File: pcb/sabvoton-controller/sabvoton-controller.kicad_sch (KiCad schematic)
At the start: 1 part

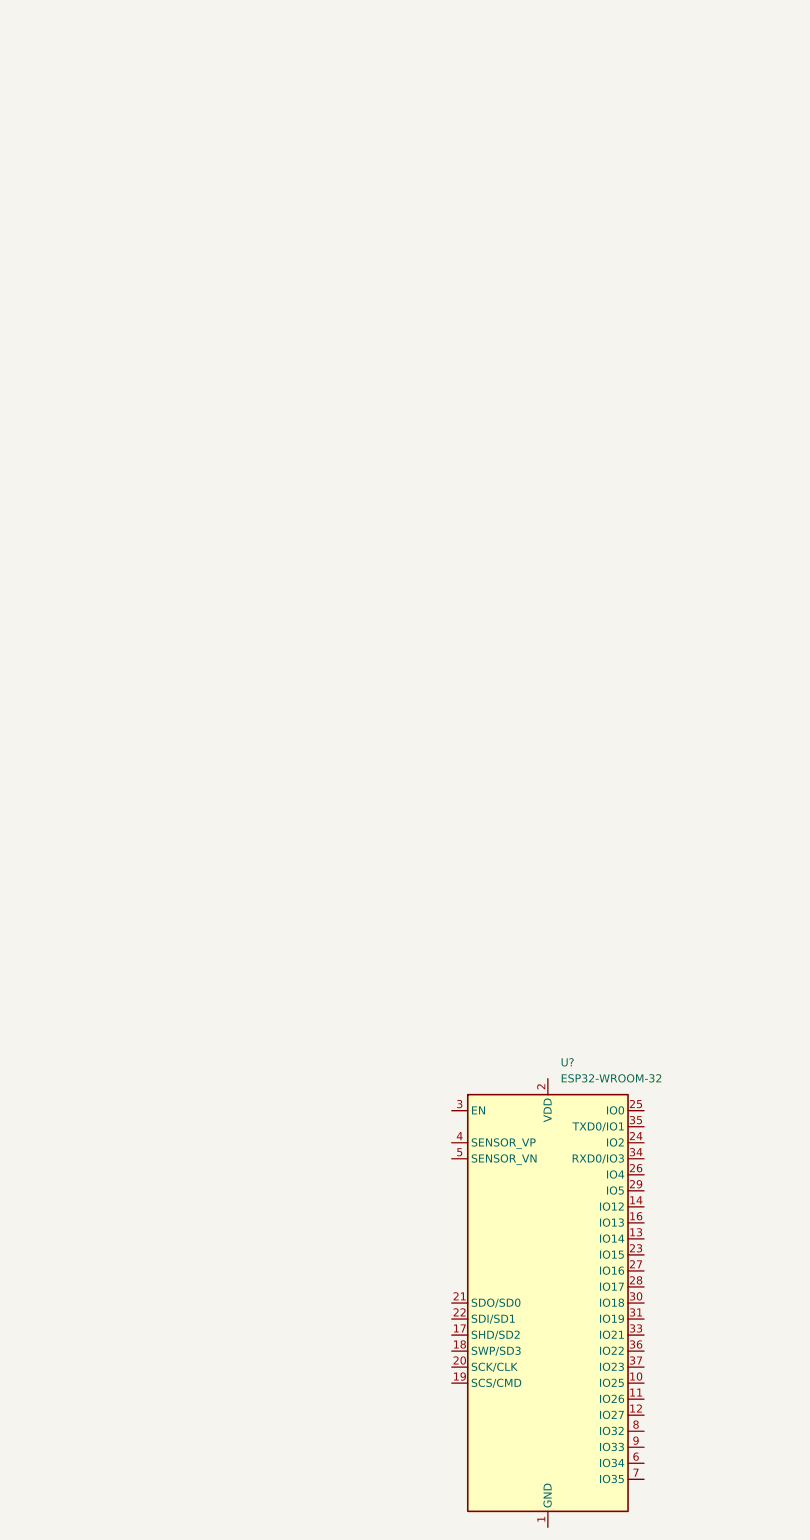
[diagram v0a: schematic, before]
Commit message: Added controller connectors && microcontroller
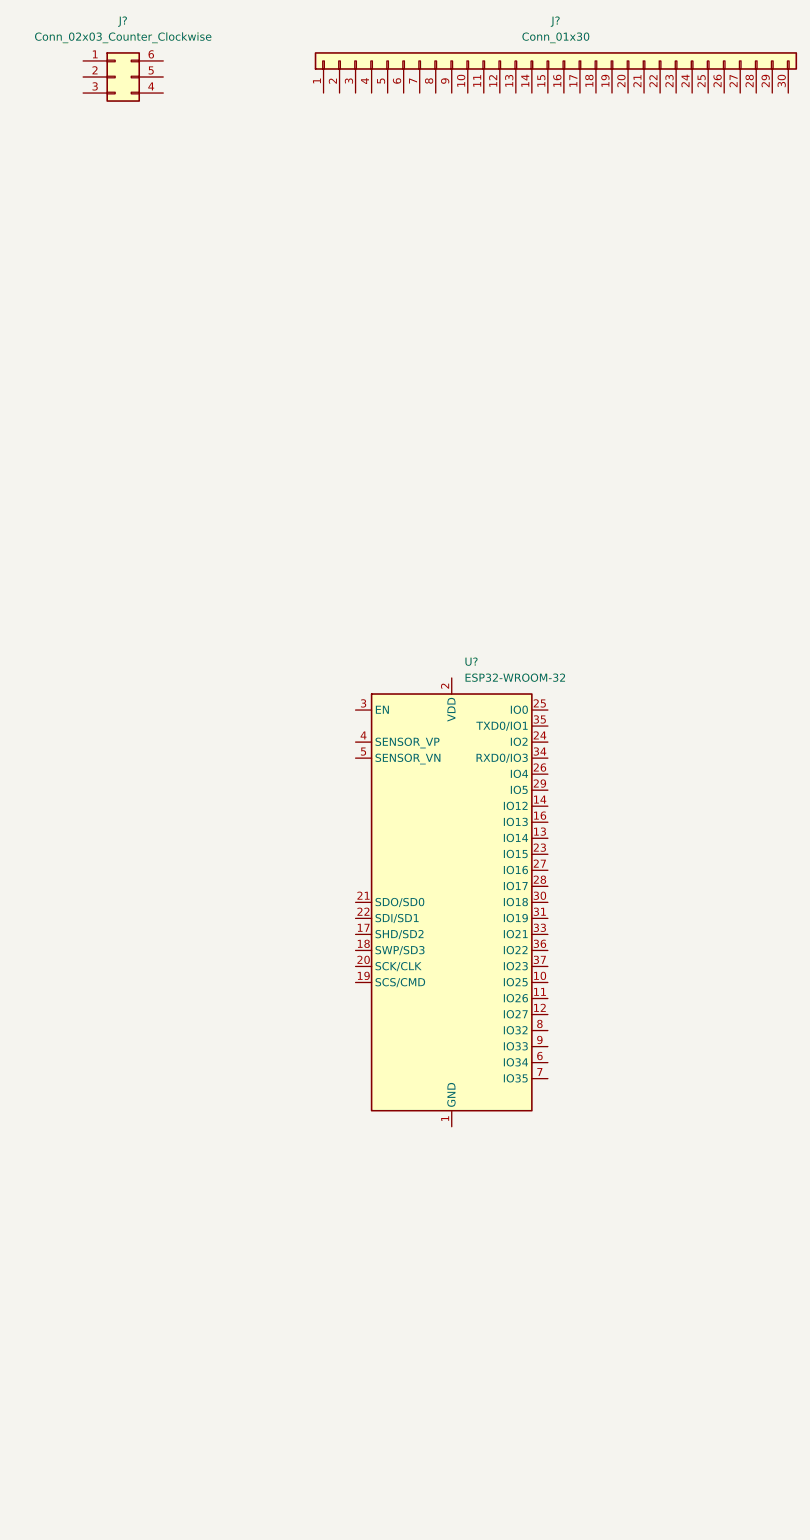
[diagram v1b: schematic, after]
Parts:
- added J?: Conn_02x03_Counter_Clockwise, symbol Connector_Generic:Conn_02x03_Counter_Clockwise
- added J?: Conn_01x30, symbol Connector_Generic:Conn_01x30
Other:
- moved on the sheet: U?
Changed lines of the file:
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@@
 (kicad_sch (version 20211123) (generator eeschema)
   (paper "A1")
-  (symbol (lib_id "RF_Module:ESP32-WROOM-32") (at 384.81 260.35 0) (unit 1)
+  (symbol (lib_id "Connector_Generic:Conn_02x03_Counter_Clockwise") (at 316.23 66.04 0) (unit 1)
     (in_bom yes) (on_board yes) (fields_autoplaced)
-    (property "Reference" "U?" (id 0) (at 386.8294 222.25 0)
+    (property "Reference" "J?" (id 0) (at 317.5 57.15 0))
+    (property "Value" "Conn_02x03_Counter_Clockwise" (id 1) (at 317.5 59.69 0))
+    (property "Footprint" "" (id 2) (at 316.23 66.04 0)
+      (effects (font (size 1.27 1.27)) hide)
+    )
+    (property "Datasheet" "~" (id 3) (at 316.23 66.04 0)
+      (effects (font (size 1.27 1.27)) hide)
+    )
+    (pin "1")
+    (pin "2")
+    (pin "3")
+    (pin "4")
+    (pin "5")
+    (pin "6")
+  )
+  (symbol (lib_id "RF_Module:ESP32-WROOM-32") (at 369.57 196.85 0) (unit 1)
+    (in_bom yes) (on_board yes) (fields_autoplaced)
+    (property "Reference" "U?" (id 0) (at 371.5894 158.75 0)
       (effects (font (size 1.27 1.27)) (justify left))
     )
-    (property "Value" "ESP32-WROOM-32" (id 1) (at 386.8294 224.79 0)
+    (property "Value" "ESP32-WROOM-32" (id 1) (at 371.5894 161.29 0)
       (effects (font (size 1.27 1.27)) (justify left))
     )
-    (property "Footprint" "RF_Module:ESP32-WROOM-32" (id 2) (at 384.81 298.45 0)
+    (property "Footprint" "RF_Module:ESP32-WROOM-32" (id 2) (at 369.57 234.95 0)
       (effects (font (size 1.27 1.27)) hide)
     )
-    (property "Datasheet" "https://www.espressif.com/sites/default/files/documentation/esp32-wroom-32_datasheet_en.pdf" (id 3) (at 377.19 259.08 0)
+    (property "Datasheet" "https://www.espressif.com/sites/default/files/documentation/esp32-wroom-32_datasheet_en.pdf" (id 3) (at 361.95 195.58 0)
       (effects (font (size 1.27 1.27)) hide)
     )
@@
     (pin "9")
   )
+  (symbol (lib_id "Connector_Generic:Conn_01x30") (at 384.81 63.5 90) (unit 1)
+    (in_bom yes) (on_board yes) (fields_autoplaced)
+    (property "Reference" "J?" (id 0) (at 386.08 57.15 90))
+    (property "Value" "Conn_01x30" (id 1) (at 386.08 59.69 90))
+    (property "Footprint" "" (id 2) (at 384.81 63.5 0)
+      (effects (font (size 1.27 1.27)) hide)
+    )
+    (property "Datasheet" "~" (id 3) (at 384.81 63.5 0)
+      (effects (font (size 1.27 1.27)) hide)
+    )
+    (pin "1")
+    (pin "10")
+    (pin "11")
+    (pin "12")
+    (pin "13")
+    (pin "14")
+    (pin "15")
+    (pin "16")
+    (pin "17")
+    (pin "18")
+    (pin "19")
+    (pin "2")
+    (pin "20")
+    (pin "21")
+    (pin "22")
+    (pin "23")
+    (pin "24")
+    (pin "25")
+    (pin "26")
+    (pin "27")
+    (pin "28")
+    (pin "29")
+    (pin "3")
+    (pin "30")
+    (pin "4")
+    (pin "5")
+    (pin "6")
+    (pin "7")
+    (pin "8")
+    (pin "9")
+  )
   (sheet_instances
     (path "/" (page "1"))
   )
   (symbol_instances
+    (path "/5cd3ea2a-358f-457f-a260-ed9cd240c7ff"
+      (reference "J?") (unit 1) (value "Conn_02x03_Counter_Clockwise") (footprint "")
+    )
+    (path "/d24c1341-da64-4d94-8395-0809e8923d83"
+      (reference "J?") (unit 1) (value "Conn_01x30") (footprint "")
+    )
     (path "/c06608e9-3454-4d79-bf69-0fdfa3419b82"
       (reference "U?") (unit 1) (value "ESP32-WROOM-32") (footprint "RF_Module:ESP32-WROOM-32")

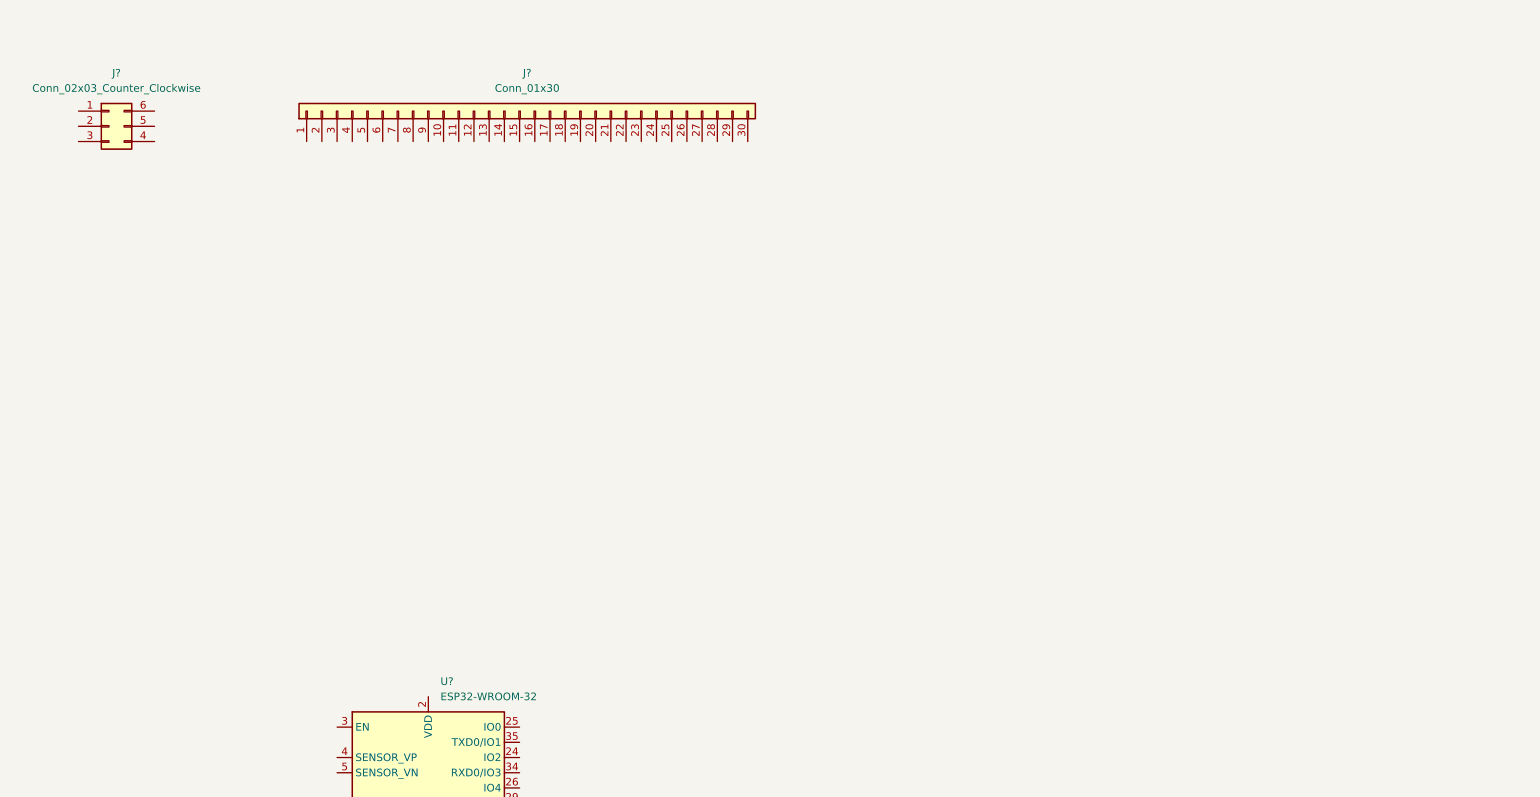
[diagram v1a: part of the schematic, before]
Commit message: Added 12V conversion part
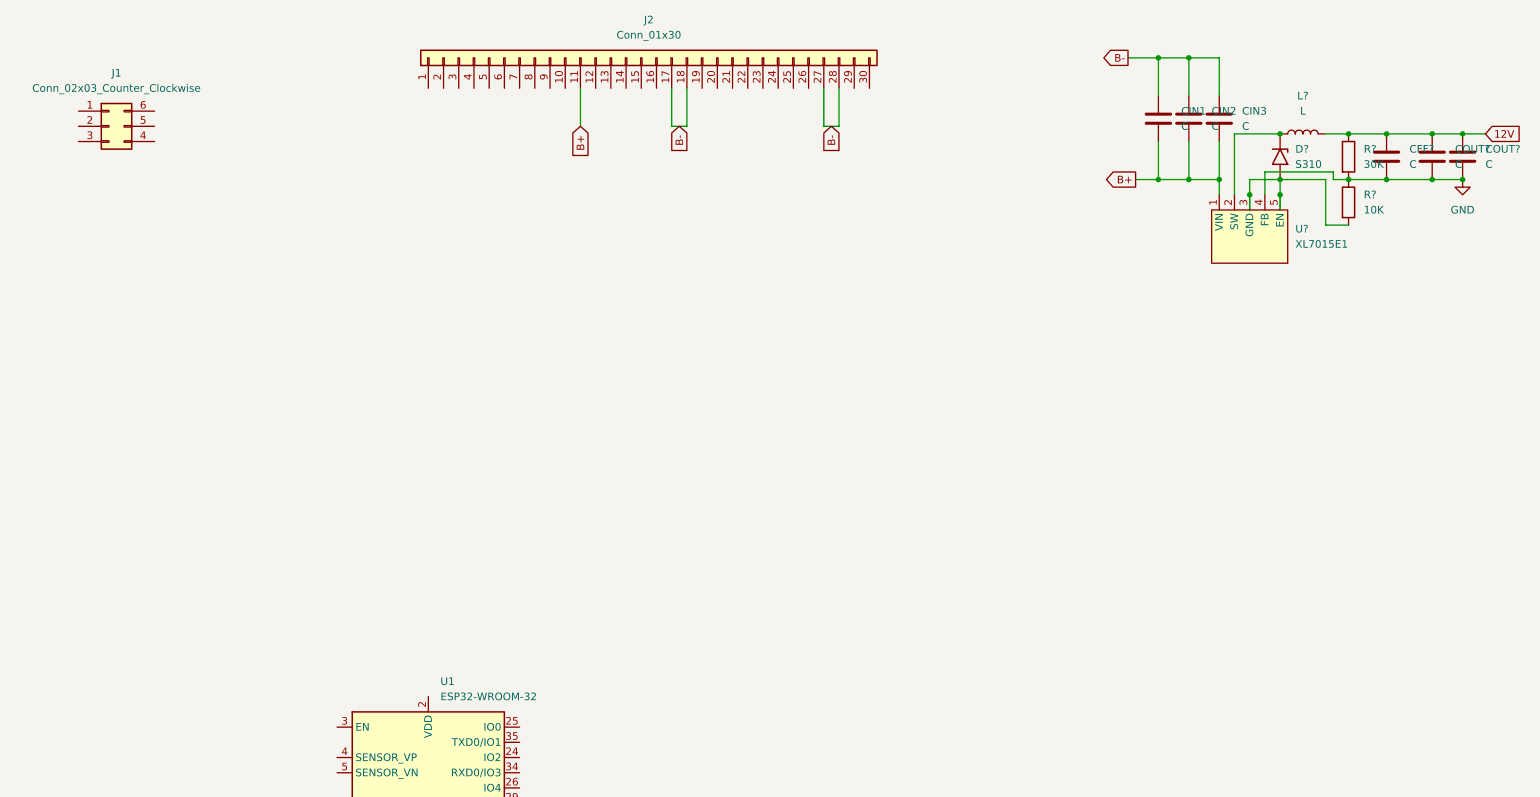
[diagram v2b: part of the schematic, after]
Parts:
- added CFF?: C, Capacitor_SMD:C_1206_3216Metric_Pad1.33x1.80mm_HandSolder, symbol Device:C
- added CIN1, CIN2, CIN3, COUT? (x2): C, Capacitor_SMD:C_1210_3225Metric_Pad1.33x2.70mm_HandSolder, symbol Device:C
- added D?: S310, KT_Display:S2M, symbol Diode:1.5KExxA
- added L?: L, Inductor_SMD:L_7.3x7.3_H3.5, symbol Device:L
- added R?: 30K, Resistor_SMD:R_1206_3216Metric_Pad1.30x1.75mm_HandSolder, symbol Device:R
- added R?: 10K, Resistor_SMD:R_1206_3216Metric_Pad1.30x1.75mm_HandSolder, symbol Device:R
- added U?: XL7015E1, Package_TO_SOT_SMD:TO-252-5_TabPin3, symbol KT_Display:XL7015E1
- gave numbers to parts that had none: 3
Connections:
- net B+: now reaches J2.11 (Pin_11)
- net B+: now also CIN1.2, CIN2.2, CIN3.2, U?.1 (VIN)
- net B-: now reaches J2.17 (Pin_17)
- net B-: now also J2.18 (Pin_18), J2.27 (Pin_27), J2.28 (Pin_28), CIN1.1, CIN2.1, CIN3.1
- new net: D?.1 (A1), L?.1, U?.2 (SW)
- new net: D?.2 (A2), R?.2, U?.3 (GND), U?.5 (EN)
- new net 12V: CFF?.2, COUT?.1, COUT?.1, L?.2, R?.1
- new net GND: CFF?.1, COUT?.2, COUT?.2, R?.1, R?.2, U?.4 (FB)
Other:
- moved on the sheet: J2

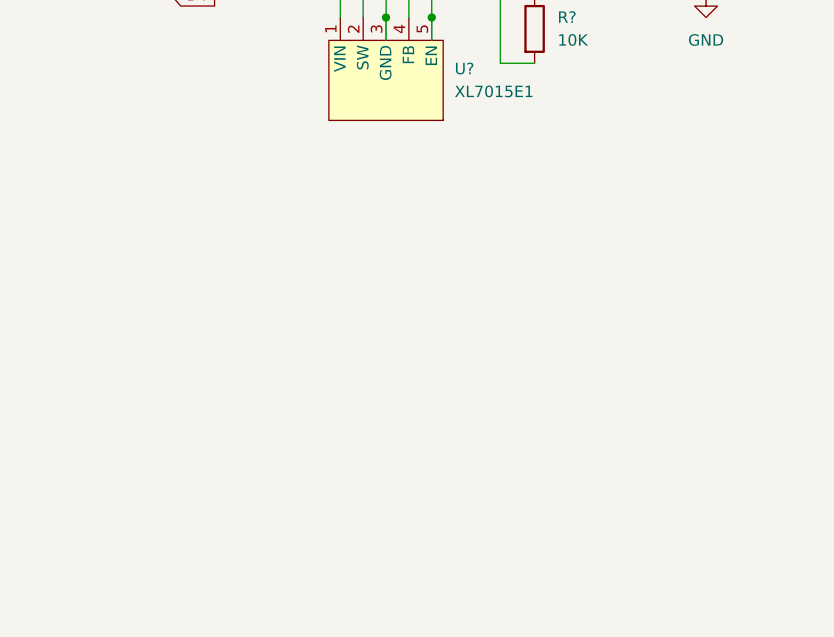
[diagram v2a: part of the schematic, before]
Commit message: Added 5V conversion part
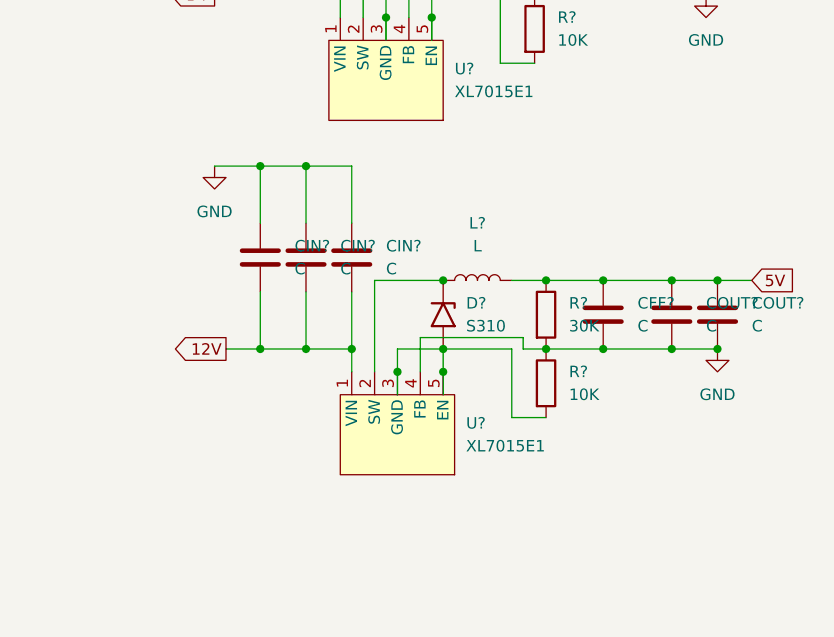
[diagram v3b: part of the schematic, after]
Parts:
- added CFF?: C, Capacitor_SMD:C_1206_3216Metric_Pad1.33x1.80mm_HandSolder, symbol Device:C
- added CIN? (x3), COUT? (x2): C, Capacitor_SMD:C_1210_3225Metric_Pad1.33x2.70mm_HandSolder, symbol Device:C
- added D?: S310, KT_Display:S2M, symbol Diode:1.5KExxA
- added L?: L, Inductor_SMD:L_7.3x7.3_H3.5, symbol Device:L
- added R?: 10K, Resistor_SMD:R_1206_3216Metric_Pad1.30x1.75mm_HandSolder, symbol Device:R
- added R?: 30K, Resistor_SMD:R_1206_3216Metric_Pad1.30x1.75mm_HandSolder, symbol Device:R
- added U?: XL7015E1, Package_TO_SOT_SMD:TO-252-5_TabPin3, symbol KT_Display:XL7015E1
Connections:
- net 12V: now also CIN?.2, CIN?.2, CIN?.2, U?.1 (VIN)
- net GND: now also CFF?.1, CIN?.1, CIN?.1, CIN?.1, COUT?.2, COUT?.2, R?.1, R?.2, U?.4 (FB)
- new net: D?.1 (A1), L?.1, U?.2 (SW)
- new net: D?.2 (A2), R?.2, U?.3 (GND), U?.5 (EN)
- new net 5V: CFF?.2, COUT?.1, COUT?.1, L?.2, R?.1

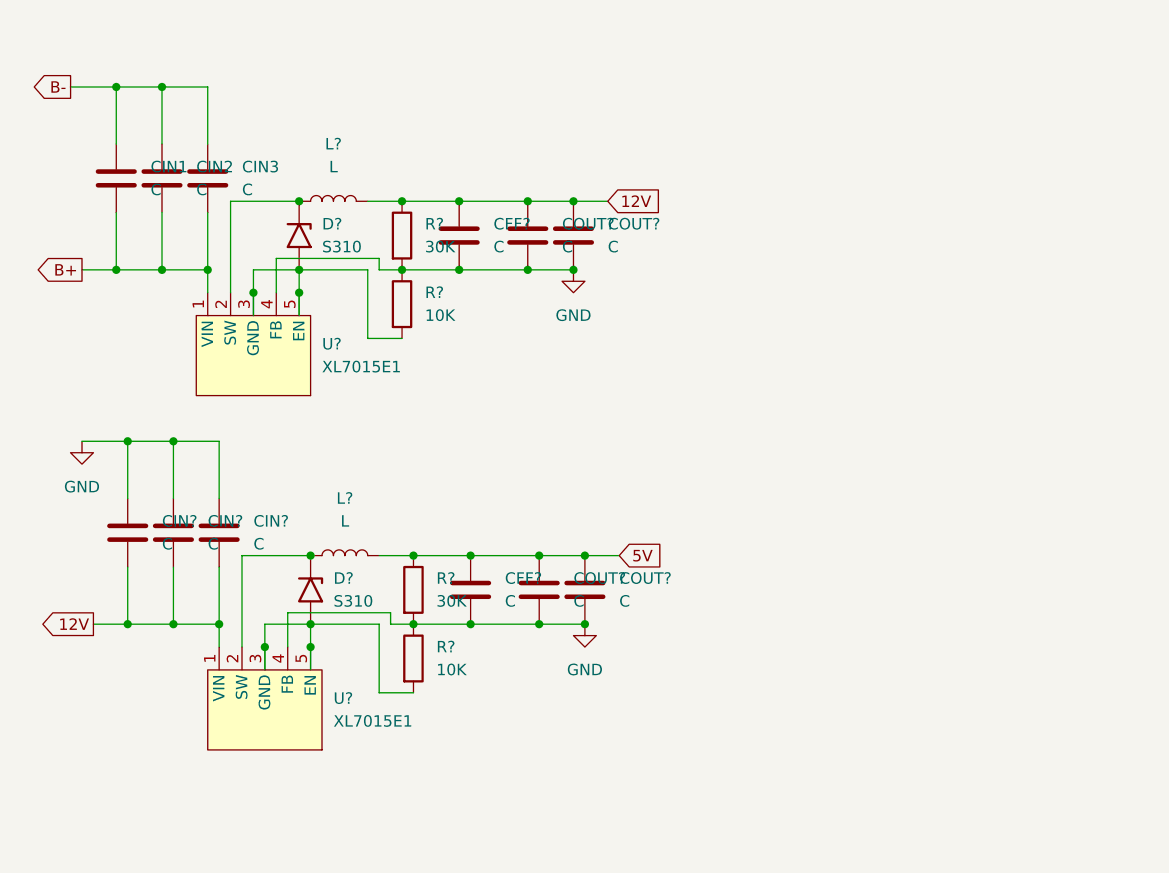
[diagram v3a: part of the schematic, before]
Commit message: Added 3.3V conversion
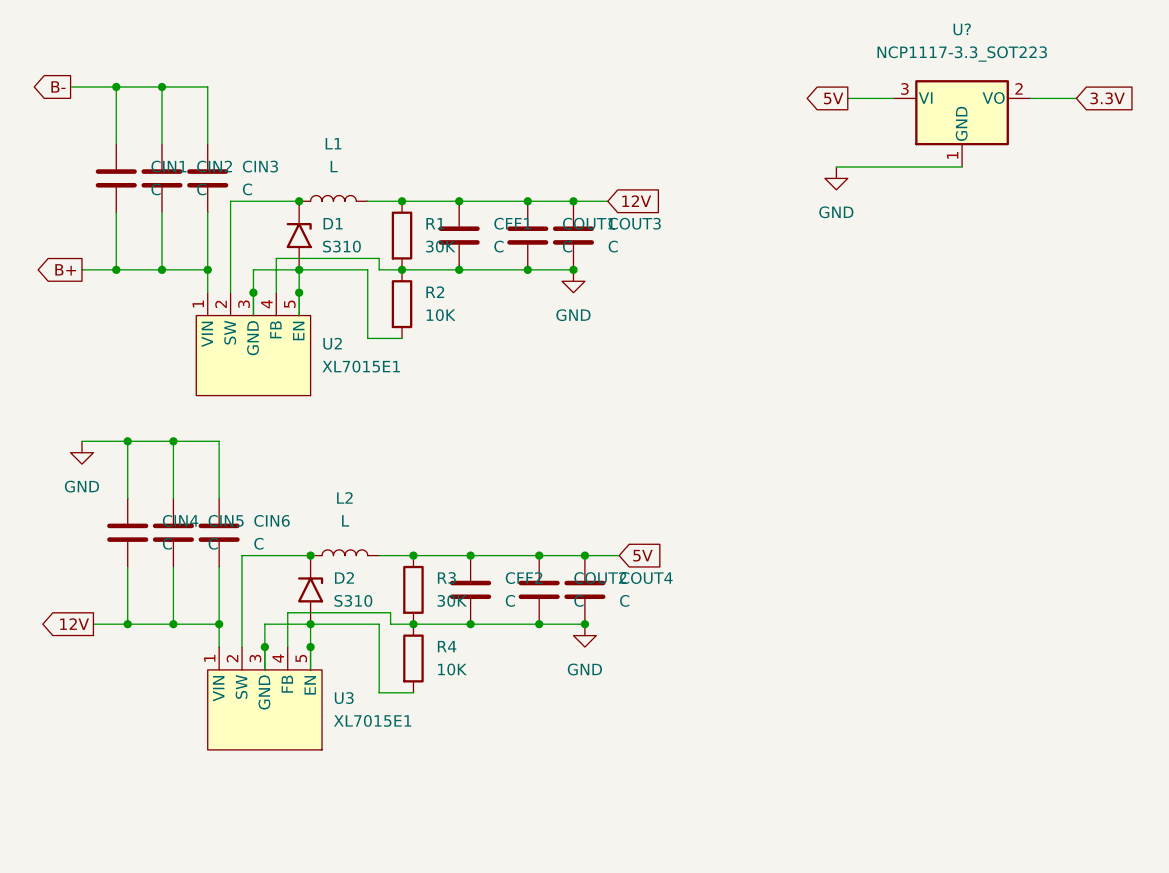
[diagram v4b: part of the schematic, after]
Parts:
- added U?: NCP1117-3.3_SOT223, Package_TO_SOT_SMD:SOT-223-3_TabPin2, symbol Regulator_Linear:NCP1117-3.3_SOT223
- gave numbers to parts that had none: 19
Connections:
- net 5V: now also U?.3 (VI)
- net GND: now also U?.1 (GND)
- new net 3.3V: U?.2 (VO)
